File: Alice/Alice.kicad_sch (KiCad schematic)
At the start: 22 parts

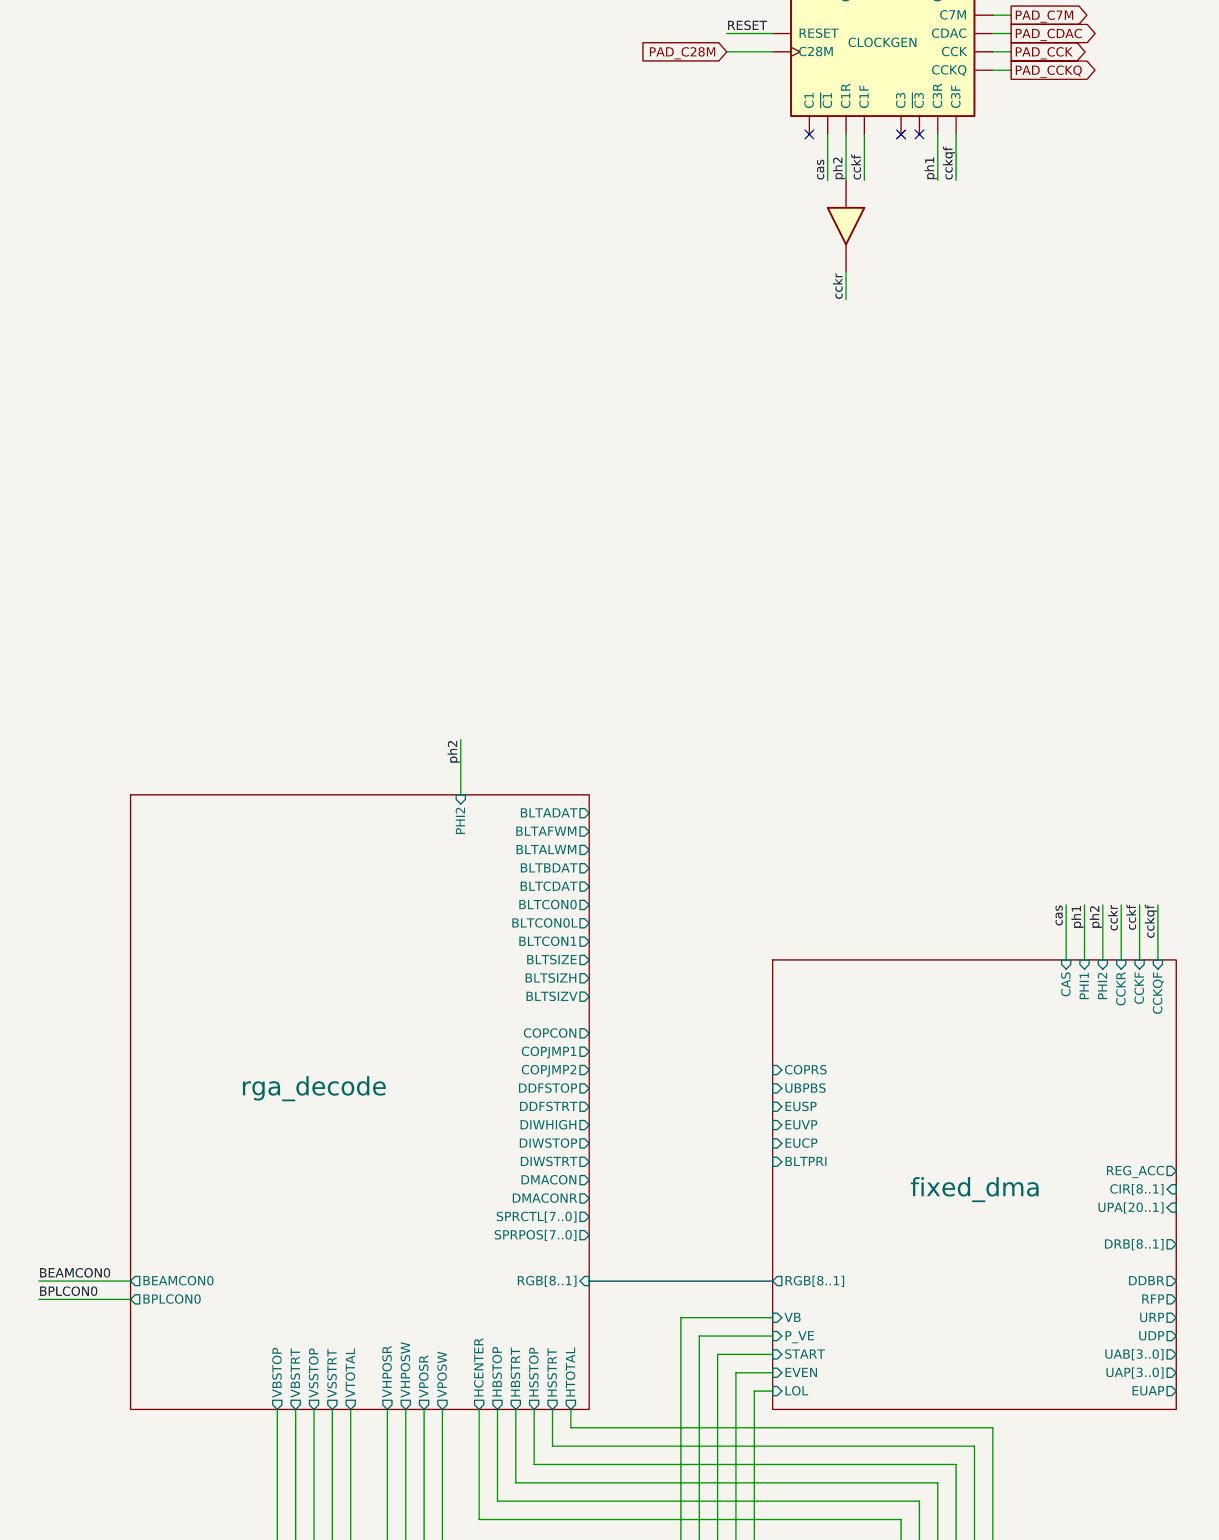
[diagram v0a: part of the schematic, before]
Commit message: Plane DMA sheet added
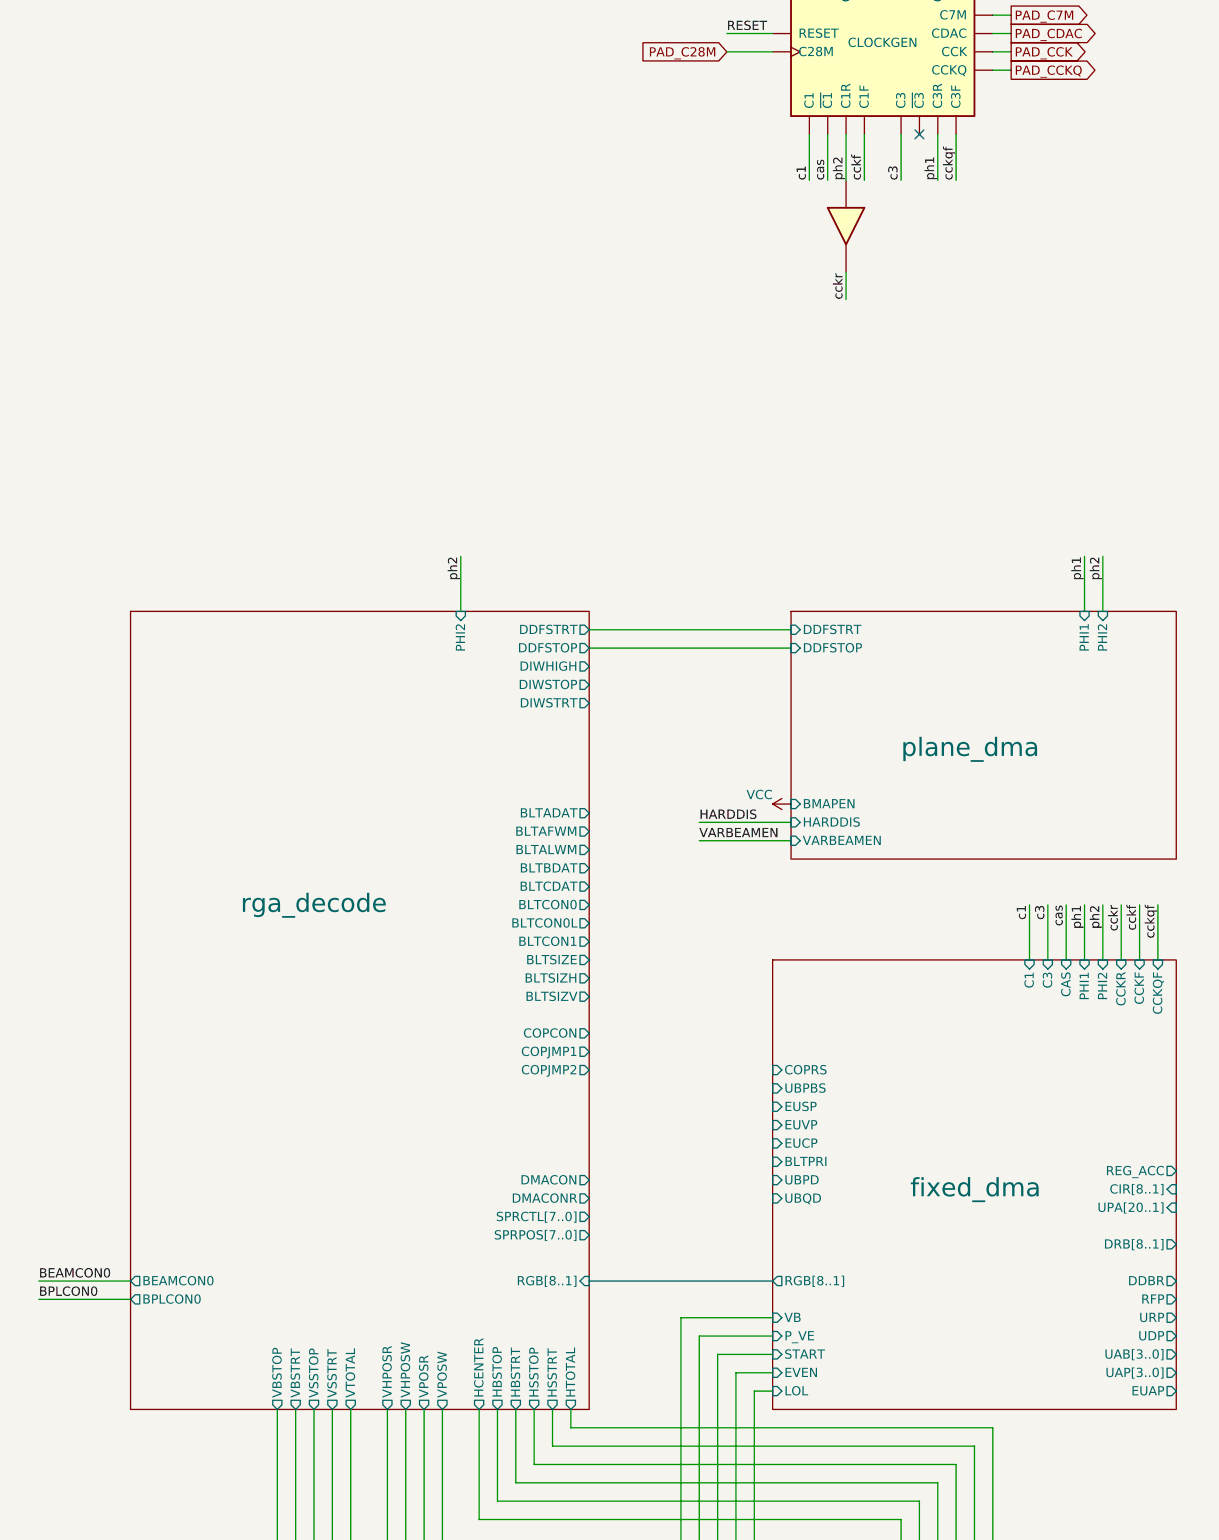
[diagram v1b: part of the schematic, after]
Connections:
- net c3: now reaches CLK1.15 (C3)
- net c1: now reaches CLK1.7 (C1)
- no-connect marks 28 -> 26
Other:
- added sheet plane_dma (plane_dma.kicad_sch)
- sheet fixed_dma ports: added C1, C3, UBPD, UBQD; removed none

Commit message: DMA bitplane sheet updated
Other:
- sheet plane_dma ports: added BSVB, DIWHIGH, DIWSTOP, DIWSTRT, VARVBEN; removed none

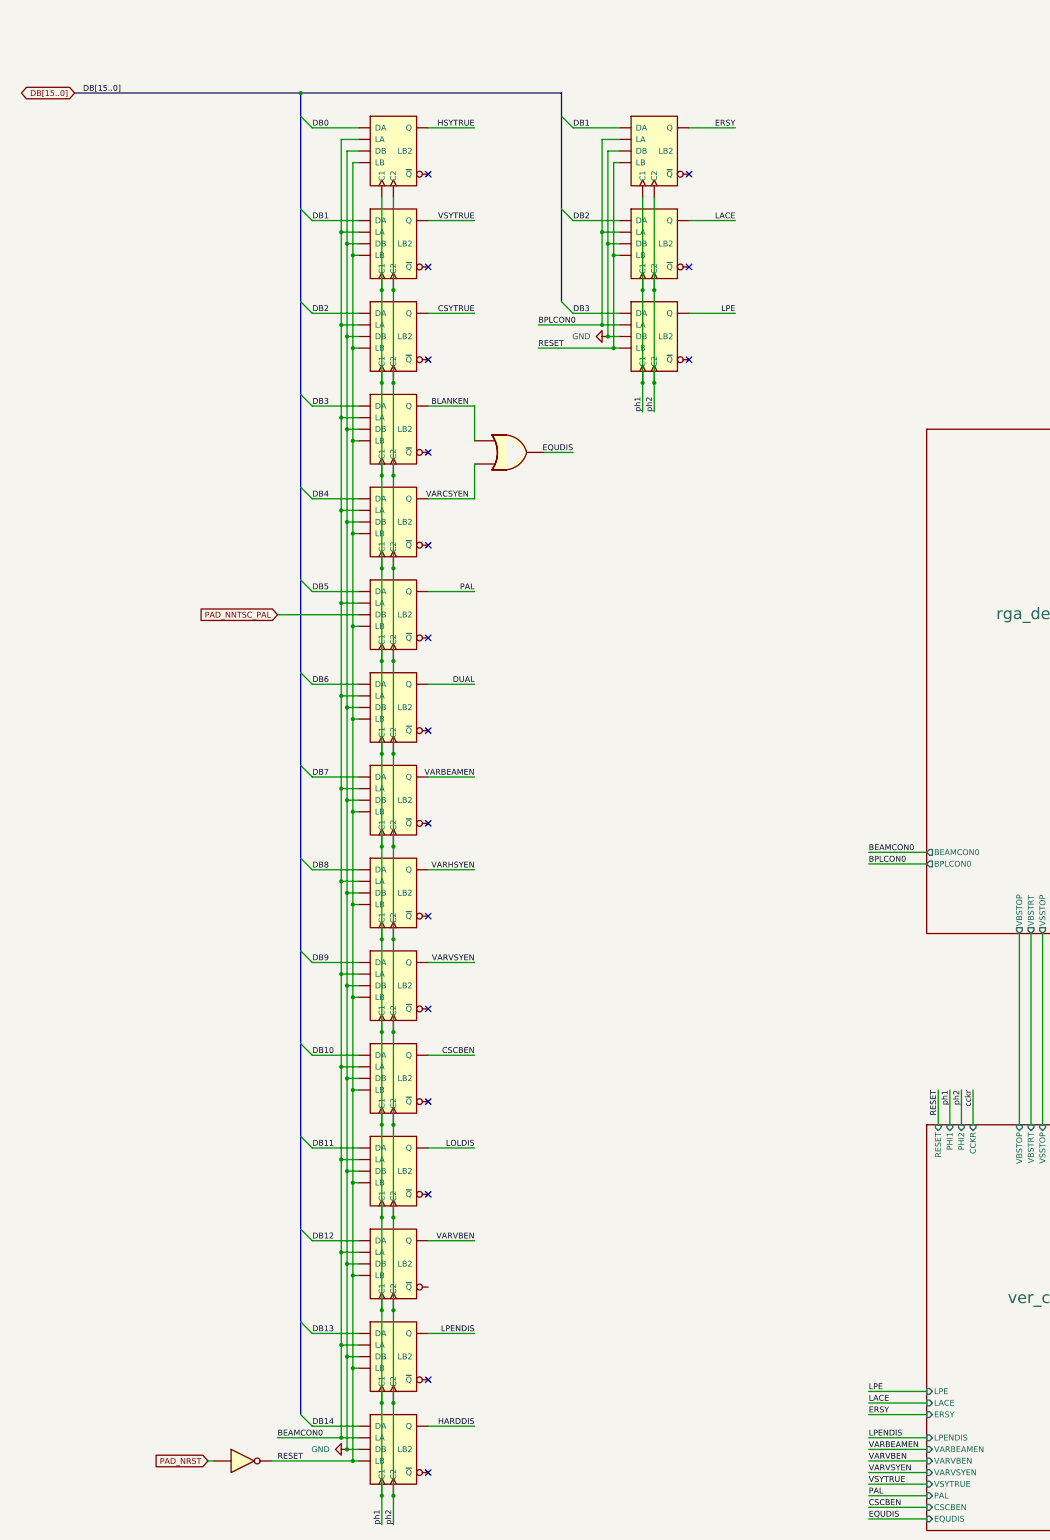
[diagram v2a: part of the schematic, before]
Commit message: BPLCON0 and FMODE registers added
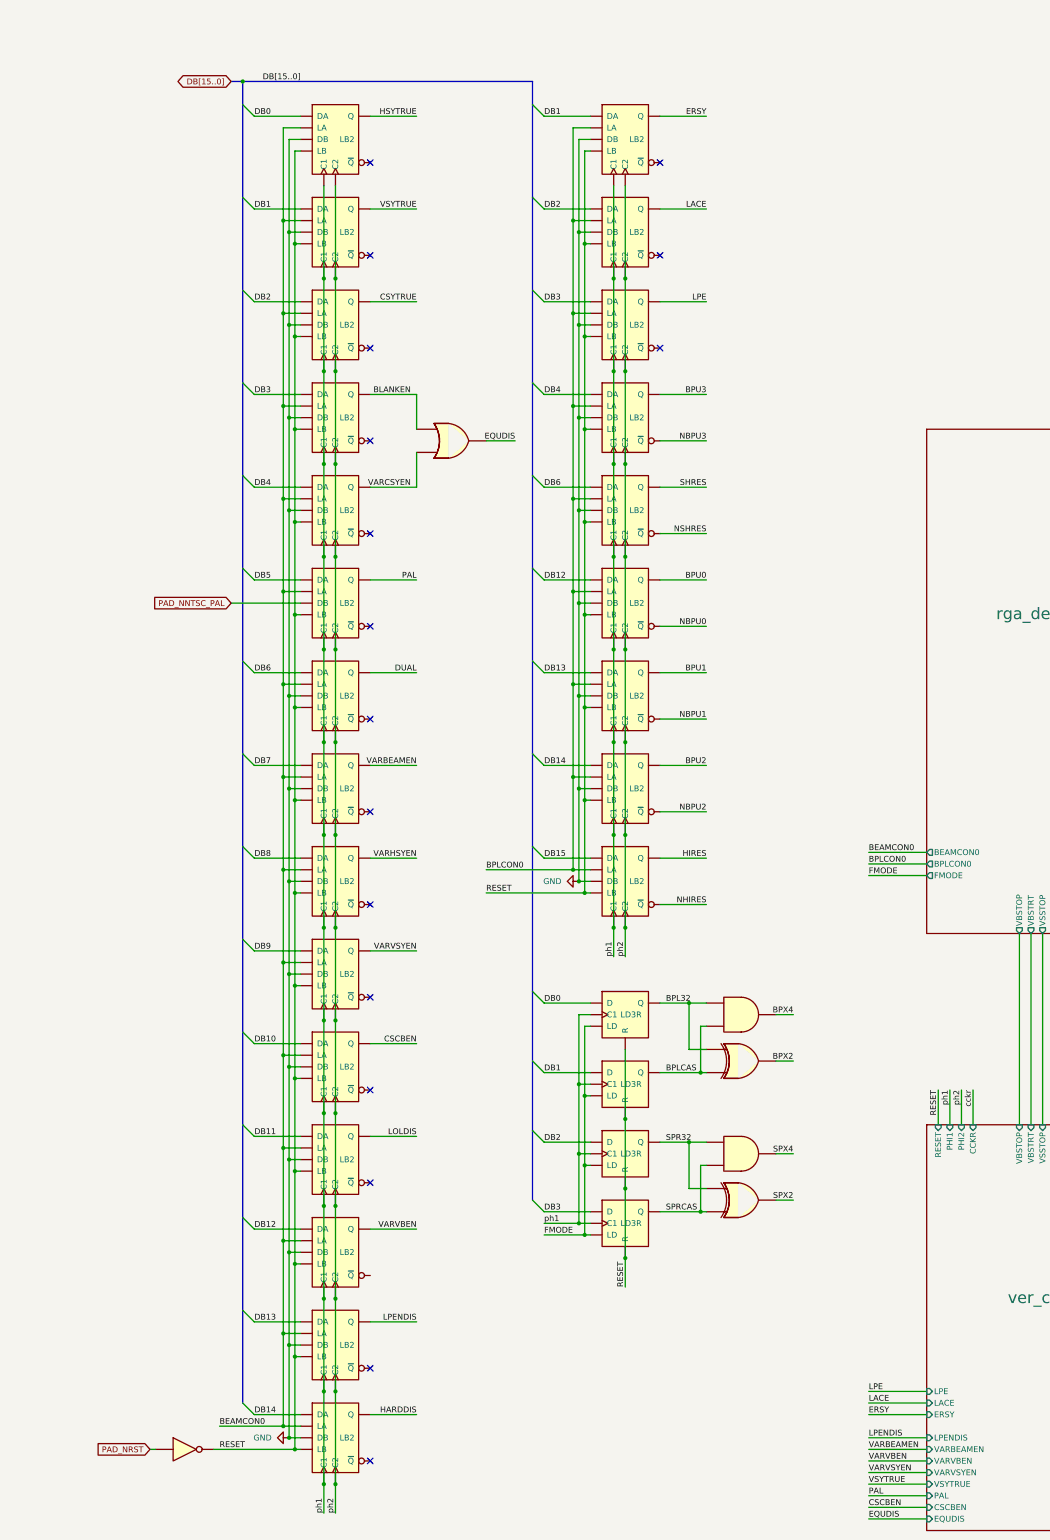
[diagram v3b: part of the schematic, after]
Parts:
- added AND_100, AND_101: AND2, symbol NMOS:AND2
- added BPLCON0_LB12, BPLCON0_LB13, BPLCON0_LB14, BPLCON0_LB15, BPLCON0_LB4, BPLCON0_LB6: LB2, symbol NMOS:LB2
- added FMODE_LD0, FMODE_LD1, FMODE_LD2, FMODE_LD3: LD3R, symbol NMOS:LD3R
- added XOR_1, XOR_2: XOR2, symbol NMOS:XOR2
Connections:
- net BPLCON0: now also BPLCON0_LB12.2 (LA), BPLCON0_LB13.2 (LA), BPLCON0_LB14.2 (LA), BPLCON0_LB15.2 (LA), BPLCON0_LB4.2 (LA), BPLCON0_LB6.2 (LA)
- net DB0: now also FMODE_LD0.3 (D)
- net DB1: now also FMODE_LD1.3 (D)
- net DB12: now also BPLCON0_LB12.1 (DA)
- net DB13: now also BPLCON0_LB13.1 (DA)
- net DB14: now also BPLCON0_LB14.1 (DA)
- net DB2: now also FMODE_LD2.3 (D)
- net DB3: now also FMODE_LD3.3 (D)
- net DB4: now also BPLCON0_LB4.1 (DA)
- net DB6: now also BPLCON0_LB6.1 (DA)
- net GND: now also BPLCON0_LB12.3 (DB), BPLCON0_LB13.3 (DB), BPLCON0_LB14.3 (DB), BPLCON0_LB15.3 (DB), BPLCON0_LB4.3 (DB), BPLCON0_LB6.3 (DB)
- net RESET: now also BPLCON0_LB12.4 (LB), BPLCON0_LB13.4 (LB), BPLCON0_LB14.4 (LB), BPLCON0_LB15.4 (LB), BPLCON0_LB4.4 (LB), BPLCON0_LB6.4 (LB), FMODE_LD0.6 (R), FMODE_LD1.6 (R), FMODE_LD2.6 (R), FMODE_LD3.6 (R)
- net ph1: now also BPLCON0_LB12.7 (C1), BPLCON0_LB13.7 (C1), BPLCON0_LB14.7 (C1), BPLCON0_LB15.7 (C1), BPLCON0_LB4.7 (C1), BPLCON0_LB6.7 (C1), FMODE_LD0.4 (C1), FMODE_LD1.4 (C1), FMODE_LD2.4 (C1), FMODE_LD3.4 (C1)
- net ph2: now also BPLCON0_LB12.8 (C2), BPLCON0_LB13.8 (C2), BPLCON0_LB14.8 (C2), BPLCON0_LB15.8 (C2), BPLCON0_LB4.8 (C2), BPLCON0_LB6.8 (C2)
- new net BPL32: AND_100.2, FMODE_LD0.1 (Q), XOR_1.2
- new net BPLCAS: AND_100.3, FMODE_LD1.1 (Q), XOR_1.3
- new net BPU0: BPLCON0_LB12.5 (Q)
- new net BPU1: BPLCON0_LB13.5 (Q)
- new net BPU2: BPLCON0_LB14.5 (Q)
- new net BPU3: BPLCON0_LB4.5 (Q)
- new net BPX2: XOR_1.1
- new net BPX4: AND_100.1
- new net DB15: BPLCON0_LB15.1 (DA)
- new net FMODE: FMODE_LD0.5 (LD), FMODE_LD1.5 (LD), FMODE_LD2.5 (LD), FMODE_LD3.5 (LD)
- new net HIRES: BPLCON0_LB15.5 (Q)
- new net NBPU0: BPLCON0_LB12.6 (~{Q})
- new net NBPU1: BPLCON0_LB13.6 (~{Q})
- new net NBPU2: BPLCON0_LB14.6 (~{Q})
- new net NBPU3: BPLCON0_LB4.6 (~{Q})
- new net NHIRES: BPLCON0_LB15.6 (~{Q})
- new net NSHRES: BPLCON0_LB6.6 (~{Q})
- new net SHRES: BPLCON0_LB6.5 (Q)
- new net SPR32: AND_101.2, FMODE_LD2.1 (Q), XOR_2.2
- new net SPRCAS: AND_101.3, FMODE_LD3.1 (Q), XOR_2.3
- new net SPX2: XOR_2.1
- new net SPX4: AND_101.1
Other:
- sheet rga_decode ports: added FMODE; removed none

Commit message: Started adding BPCYC16 and BPCYC32 logic for AGA fetch modes
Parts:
- removed BPLCON0_LB1, BPLCON0_LB12, BPLCON0_LB13, BPLCON0_LB14, BPLCON0_LB15, BPLCON0_LB2, BPLCON0_LB3, BPLCON0_LB4, BPLCON0_LB6: LB2, symbol NMOS:LB2
- added AND_102, AND_103, AND_104, AND_105, AND_106: AND2, symbol NMOS:AND2
- added BPLCON0_LD1, BPLCON0_LD12, BPLCON0_LD13, BPLCON0_LD14, BPLCON0_LD15, BPLCON0_LD2, BPLCON0_LD3, BPLCON0_LD4, BPLCON0_LD6: LD3R, symbol NMOS:LD3R
- added NOR_29, NOR_30, NOR_31: NOR2, symbol NMOS:NOR2
- added OR_32: OR2, symbol NMOS:OR2
- added SH_MUX1: MUX, symbol NMOS:MUX
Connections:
- net BPLCON0: now also BPLCON0_LD1.5 (LD), BPLCON0_LD12.5 (LD), BPLCON0_LD13.5 (LD), BPLCON0_LD14.5 (LD), BPLCON0_LD15.5 (LD), BPLCON0_LD2.5 (LD), BPLCON0_LD3.5 (LD), BPLCON0_LD4.5 (LD), BPLCON0_LD6.5 (LD)
- net BPU0: now also BPLCON0_LD12.1 (Q)
- net BPU1: now also BPLCON0_LD13.1 (Q)
- net BPU2: now also BPLCON0_LD14.1 (Q)
- net BPU3: now also BPLCON0_LD4.1 (Q)
- net BPX2: now also AND_106.2, NOR_30.3, SH_MUX1.2 (SEL)
- net BPX4: now also AND_104.3, AND_105.2, NOR_29.2, NOR_30.2
- net DB1: now also BPLCON0_LD1.3 (D)
- net DB12: now also BPLCON0_LD12.3 (D)
- net DB13: now also BPLCON0_LD13.3 (D)
- net DB14: now also BPLCON0_LD14.3 (D)
- net DB15: now also BPLCON0_LD15.3 (D)
- net DB2: now also BPLCON0_LD2.3 (D)
- net DB3: now also BPLCON0_LD3.3 (D)
- net DB4: now also BPLCON0_LD4.3 (D)
- net DB6: now also BPLCON0_LD6.3 (D)
- net ERSY: now also BPLCON0_LD1.1 (Q)
- net HIRES: now also AND_105.3, BPLCON0_LD15.1 (Q), NOR_31.3, SH_MUX1.4 (D0)
- net LACE: now also BPLCON0_LD2.1 (Q)
- net LPE: now also BPLCON0_LD3.1 (Q)
- net NBPU0: now also BPLCON0_LD12.2 (~{Q})
- net NBPU1: now also BPLCON0_LD13.2 (~{Q})
- net NBPU2: now also BPLCON0_LD14.2 (~{Q})
- net NBPU3: now also BPLCON0_LD4.2 (~{Q})
- net NHIRES: now also AND_102.1
- net NSHRES: now also AND_103.1
- net RESET: now also BPLCON0_LD1.6 (R), BPLCON0_LD12.6 (R), BPLCON0_LD13.6 (R), BPLCON0_LD14.6 (R), BPLCON0_LD15.6 (R), BPLCON0_LD2.6 (R), BPLCON0_LD3.6 (R), BPLCON0_LD4.6 (R), BPLCON0_LD6.6 (R)
- net SHRES: now also AND_103.2, BPLCON0_LD6.1 (Q), NOR_29.3, NOR_31.2, SH_MUX1.3 (D1)
- net ph1: now also BPLCON0_LD1.4 (C1), BPLCON0_LD12.4 (C1), BPLCON0_LD13.4 (C1), BPLCON0_LD14.4 (C1), BPLCON0_LD15.4 (C1), BPLCON0_LD2.4 (C1), BPLCON0_LD3.4 (C1), BPLCON0_LD4.4 (C1), BPLCON0_LD6.4 (C1)
- new net: AND_102.3, NOR_29.1
- new net: AND_103.3, NOR_30.1
- new net: AND_102.2, SH_MUX1.1 (S)
- new net: AND_106.1, OR_32.3
- new net: AND_105.1, OR_32.2
- new net BPCYC16: OR_32.1
- new net BPCYC32: AND_104.1
- new net LORES: AND_104.2, AND_106.3, NOR_31.1
- no-connect marks 26 -> 32
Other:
- sheet plane_dma ports: added BPCYC16, BPCYC32, BPU[3..0], HIRES, LORES, NBPU[3..0], NHIRES, NSHRES, SHRES; removed none
